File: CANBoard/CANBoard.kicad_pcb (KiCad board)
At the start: 4 copper layers, 40 x 40 mm, 83 parts, among them J1 Conn_01x08, J2 Conn_01x08, J3 Conn_01x08, J4 Conn_01x08, J5 TC2030, Q1 DMN2004WK, Q2 DMN2004WK, Q3 DMN2004WK, Q4 DMN2004WK, U1 TPS56339DDCR, U2 LD1117S33CTR, U3 MCP2562, U4 STM32F303K8T6, Y1 8mHz

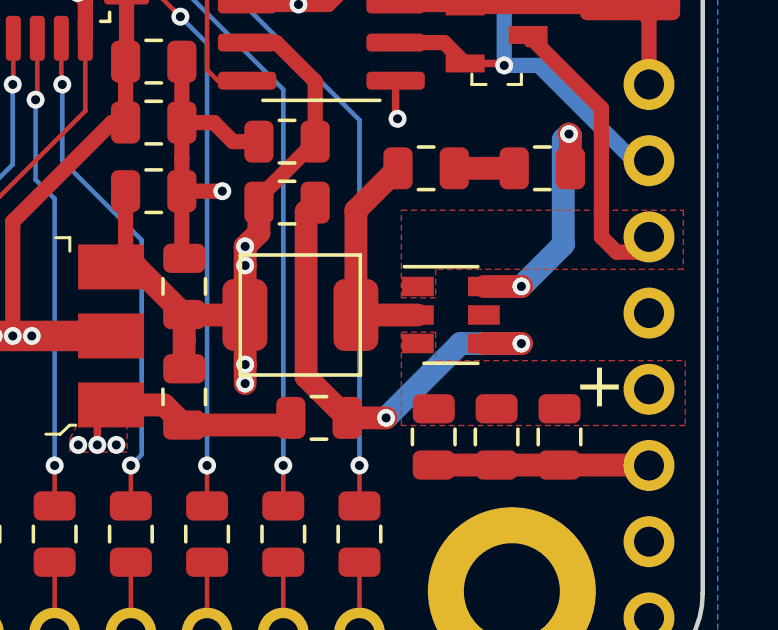
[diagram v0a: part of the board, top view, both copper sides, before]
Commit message: #12 Removed U1 EN pin 5, updated documentation
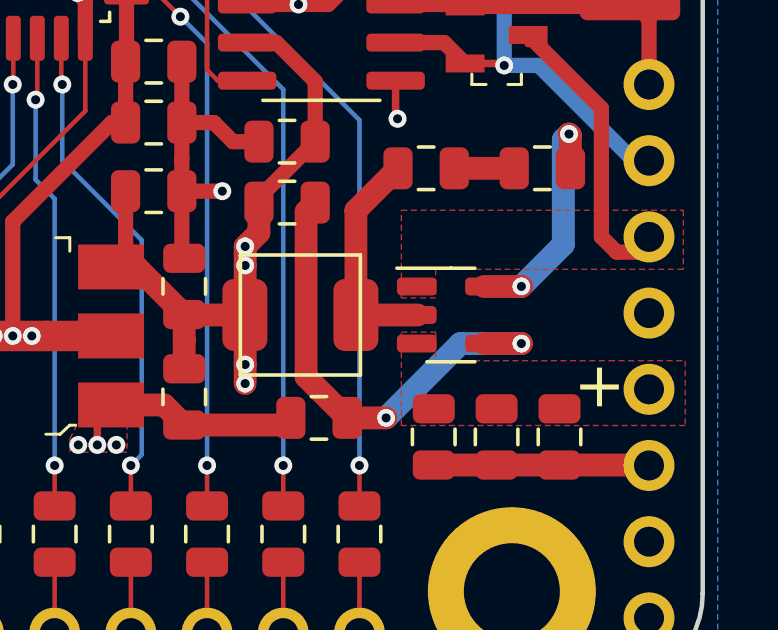
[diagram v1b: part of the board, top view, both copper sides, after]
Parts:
- U1: footprint Package_TO_SOT_SMD:SOT-23-6 -> TO_SOT_SMD_Modify:SOT-23-6_NoPin5
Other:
- board text added: "0 0 0x640 1 0 0x650 0 1 0x660 1 1 0x670"
- board text added: "1 2 Base ID"
- board text removed: "0 0 0x640 1 0 0x641 0 1 0x642 1 1 0x643"
- board text removed: "1 2 ID"
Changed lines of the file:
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@@
   (net 63 "Net-(U1-FB)")
   (net 64 "Net-(U4-BOOT0)")
-  (net 65 "unconnected-(U1-EN-Pad5)")
   (footprint "Resistor_SMD:R_0805_2012Metric" (layer "F.Cu")
     (at 144.018 97.917 -90)
@@
     (descr "LQFP, 32 Pin (https://www.nxp.com/docs/en/package-information/SOT358-1.pdf), generated with kicad-footprint-generator ipc_gullwing_generator.py")
     (tags "LQFP QFP")
-    (property "Digi-Key_PN" "497-13318-ND")
+    (property "Digi-Key_PN" "497-15828-ND")
     (property "LCSC" "C118318")
     (property "Sheetfile" "MCU.kicad_sch")
@@
     )
   )
-  (footprint "Package_TO_SOT_SMD:SOT-23-6" (layer "F.Cu")
+  (footprint "TO_SOT_SMD_Modify:SOT-23-6_NoPin5" (layer "F.Cu")
     (at 149.606 90.6145)
-    (descr "6-pin SOT-23 package")
-    (tags "SOT-23-6")
+    (descr "SOT, 6 Pin (https://www.jedec.org/sites/default/files/docs/Mo-178c.PDF variant AB), generated with kicad-footprint-generator ipc_gullwing_generator.py")
+    (tags "SOT TO_SOT_SMD")
     (property "Digi-Key_PN" "296-53568-1-ND")
     (property "LCSC" "C2071106")
@@
     (property "Sheetname" "")
     (attr smd)
-    (fp_text reference "U1" (at 0 -2.9) (layer "F.SilkS") hide
+    (fp_text reference "U1" (at 0 -2.4) (layer "F.SilkS") hide
         (effects (font (size 1 1) (thickness 0.15)))
     )
-    (fp_text value "TPS56339DDCR" (at 0 2.9) (layer "F.Fab") hide
+    (fp_text value "TPS56339DDCR" (at 0 2.4) (layer "F.Fab") hide
         (effects (font (size 1 1) (thickness 0.15)))
     )
-    (fp_text user "${REFERENCE}" (at 0 0 90) (layer "F.Fab")
-        (effects (font (size 0.5 0.5) (thickness 0.075)))
+    (fp_text user "${REFERENCE}" (at 0 0) (layer "F.Fab")
+        (effects (font (size 0.4 0.4) (thickness 0.06)))
     )
-    (fp_line (start -0.9 1.61) (end 0.9 1.61)
+    (fp_line (start 0 -1.56) (end -1.8 -1.56)
+      (stroke (width 0.12) (type solid)) (layer "F.SilkS"))
+    (fp_line (start 0 -1.56) (end 0.8 -1.56)
+      (stroke (width 0.12) (type solid)) (layer "F.SilkS"))
+    (fp_line (start 0 1.56) (end -0.8 1.56)
       (stroke (width 0.12) (type solid)) (layer "F.SilkS"))
-    (fp_line (start 0.9 -1.61) (end -1.55 -1.61)
+    (fp_line (start 0 1.56) (end 0.8 1.56)
       (stroke (width 0.12) (type solid)) (layer "F.SilkS"))
-    (fp_line (start -1.9 -1.8) (end -1.9 1.8)
+    (fp_line (start -2.05 -1.7) (end -2.05 1.7)
       (stroke (width 0.05) (type solid)) (layer "F.CrtYd"))
-    (fp_line (start -1.9 1.8) (end 1.9 1.8)
+    (fp_line (start -2.05 1.7) (end 2.05 1.7)
       (stroke (width 0.05) (type solid)) (layer "F.CrtYd"))
-    (fp_line (start 1.9 -1.8) (end -1.9 -1.8)
+    (fp_line (start 2.05 -1.7) (end -2.05 -1.7)
       (stroke (width 0.05) (type solid)) (layer "F.CrtYd"))
-    (fp_line (start 1.9 1.8) (end 1.9 -1.8)
+    (fp_line (start 2.05 1.7) (end 2.05 -1.7)
       (stroke (width 0.05) (type solid)) (layer "F.CrtYd"))
-    (fp_line (start -0.9 -0.9) (end -0.9 1.55)
+    (fp_line (start -0.8 -1.05) (end -0.4 -1.45)
       (stroke (width 0.1) (type solid)) (layer "F.Fab"))
-    (fp_line (start -0.9 -0.9) (end -0.25 -1.55)
+    (fp_line (start -0.8 1.45) (end -0.8 -1.05)
       (stroke (width 0.1) (type solid)) (layer "F.Fab"))
-    (fp_line (start 0.9 -1.55) (end -0.25 -1.55)
+    (fp_line (start -0.4 -1.45) (end 0.8 -1.45)
       (stroke (width 0.1) (type solid)) (layer "F.Fab"))
-    (fp_line (start 0.9 -1.55) (end 0.9 1.55)
+    (fp_line (start 0.8 -1.45) (end 0.8 1.45)
       (stroke (width 0.1) (type solid)) (layer "F.Fab"))
-    (fp_line (start 0.9 1.55) (end -0.9 1.55)
+    (fp_line (start 0.8 1.45) (end -0.8 1.45)
       (stroke (width 0.1) (type solid)) (layer "F.Fab"))
-    (pad "1" smd rect (at -1.1 -0.95) (size 1.06 0.65) (layers "F.Cu" "F.Paste" "F.Mask")
+    (pad "1" smd roundrect (at -1.1375 -0.95) (size 1.325 0.6) (layers "F.Cu" "F.Paste" "F.Mask") (roundrect_rratio 0.25)
       (net 2 "GND") (pinfunction "GND") (pintype "power_in"))
-    (pad "2" smd rect (at -1.1 0) (size 1.06 0.65) (layers "F.Cu" "F.Paste" "F.Mask")
+    (pad "2" smd roundrect (at -1.1375 0) (size 1.325 0.6) (layers "F.Cu" "F.Paste" "F.Mask") (roundrect_rratio 0.25)
       (net 4 "Net-(U1-SW)") (pinfunction "SW") (pintype "input"))
-    (pad "3" smd rect (at -1.1 0.95) (size 1.06 0.65) (layers "F.Cu" "F.Paste" "F.Mask")
+    (pad "3" smd roundrect (at -1.1375 0.95) (size 1.325 0.6) (layers "F.Cu" "F.Paste" "F.Mask") (roundrect_rratio 0.25)
       (net 15 "+12V") (pinfunction "VIN") (pintype "power_in"))
-    (pad "4" smd rect (at 1.1 0.95) (size 1.06 0.65) (layers "F.Cu" "F.Paste" "F.Mask")
+    (pad "4" smd roundrect (at 1.1375 0.95) (size 1.325 0.6) (layers "F.Cu" "F.Paste" "F.Mask") (roundrect_rratio 0.25)
       (net 63 "Net-(U1-FB)") (pinfunction "FB") (pintype "input"))
-    (pad "5" smd rect (at 1.1 0) (size 1.06 0.65) (layers "F.Cu" "F.Paste" "F.Mask")
-      (net 65 "unconnected-(U1-EN-Pad5)") (pinfunction "EN") (pintype "input+no_connect"))
-    (pad "6" smd rect (at 1.1 -0.95) (size 1.06 0.65) (layers "F.Cu" "F.Paste" "F.Mask")
+    (pad "6" smd roundrect (at 1.1375 -0.95) (size 1.325 0.6) (layers "F.Cu" "F.Paste" "F.Mask") (roundrect_rratio 0.25)
       (net 62 "Net-(U1-BOOT)") (pinfunction "BOOT") (pintype "input"))
-    (model "${KISYS3DMOD}/Package_TO_SOT_SMD.3dshapes/SOT-23-6.wrl"
+    (model "${KICAD6_3DMODEL_DIR}/Package_TO_SOT_SMD.3dshapes/SOT-23-6.wrl"
       (offset (xyz 0 0 0))
       (scale (xyz 1 1 1))
@@
   (gr_line (start 155.956 75.6285) (end 155.956 81.3435)
     (stroke (width 0.12) (type default)) (layer "B.SilkS"))
-  (gr_line (start 157.226 76.5937) (end 150.241 76.5937)
+  (gr_line (start 157.226 76.5937) (end 149.606 76.5937)
     (stroke (width 0.12) (type default)) (layer "B.SilkS"))
   (gr_line (start 154.94 101.854) (end 154.94 94.742)
@@
     (effects (font (size 1.5 1.5) (thickness 0.3)) (justify right mirror))
   )
-  (gr_text "0  0  0x640\n1  0  0x641\n0  1  0x642\n1  1  0x643" (at 157.099 79.121) (layer "B.SilkS")
+  (gr_text "0  0  0x640\n1  0  0x650\n0  1  0x660\n1  1  0x670" (at 157.099 79.121) (layer "B.SilkS")
     (effects (font (size 0.75 0.75) (thickness 0.15)) (justify left mirror))
   )
@@
     (effects (font (size 0.75 0.75) (thickness 0.15)) (justify left mirror))
   )
-  (gr_text "1  2  ID" (at 157.099 76.1365) (layer "B.SilkS")
+  (gr_text "1  2  Base ID" (at 157.099 76.1365) (layer "B.SilkS")
     (effects (font (size 0.75 0.75) (thickness 0.15) bold) (justify left mirror))
   )
